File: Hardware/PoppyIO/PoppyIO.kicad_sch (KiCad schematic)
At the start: 244 parts, among them U11 74HC14, U12 74HC14

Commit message: hw: io: Different fuses
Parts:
- C29: value 100n -> (none); footprint Capacitor_SMD:C_0603_1608Metric_Pad1.08x0.95mm_HandSolder -> (none)
- F1, F10, F11, F12, F13, F14, F15, F16, F2, F3, F4, F5, F6, F7, F8, F9: Reichelt SKU PTC FSMD0302920R -> LITT 1210L010WR
- R74: footprint Resistor_SMD:R_0603_1608Metric -> (none)
- R75, R76, R77, R78, R79, R80, R81, R82, R83, R84, R85, R86, R87, R88, R89: value 10k -> (none); footprint Resistor_SMD:R_0603_1608Metric -> (none)
- U10, U11, U12: value 74HC14 -> (none); footprint Package_SO:SOIC-14_3.9x8.7mm_P1.27mm -> (none)
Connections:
- net O00_FIELD: now also F1.2; no longer F7.2
- net O01_FIELD: now also F2.2; no longer F6.2
- net O02_FIELD: now also F3.2; no longer F5.2
- net O04_FIELD: now also F5.2; no longer F3.2
- net O05_FIELD: now also F6.2; no longer F2.2
- net O06_FIELD: now also F7.2; no longer F1.2
- net O07_FIELD: now also F8.2; no longer F12.2
- net O08_FIELD: now also F9.2; no longer F11.2
- net O10_FIELD: now also F11.2; no longer F9.2
- net O11_FIELD: now also F12.2; no longer F8.2
- net O12_FIELD: now also F13.2; no longer F16.2
- net O13_FIELD: now also F14.2; no longer F15.2
- net O14_FIELD: now also F15.2; no longer F14.2
- net O15_FIELD: now also F16.2; no longer F13.2
- net at F11.1: now also U7.13 (O4); no longer U7.11 (O6)
- net at F6.1: now also U6.15 (O2); no longer U6.11 (O6)
- net at F8.1: now also U7.10 (O7); no longer U7.14 (O3)
- net at F13.1: now also U8.13 (O4); no longer U8.16 (O1)
- net at U6.10 (O7): now also F1.1; no longer F7.1
- net at U6.12 (O5): now also F3.1; no longer F5.1
- net at U6.14 (O3): now also F5.1; no longer F3.1
- net at F2.1: now also U6.11 (O6); no longer U6.15 (O2)
- net at U6.16 (O1): now also F7.1; no longer F1.1
- net at F15.1: now also U8.15 (O2); no longer U8.14 (O3)
- net at F14.1: now also U8.14 (O3); no longer U8.15 (O2)
- net at F16.1: now also U8.16 (O1); no longer U8.13 (O4)
- net at F12.1: now also U7.14 (O3); no longer U7.10 (O7)
- net at F9.1: now also U7.11 (O6); no longer U7.13 (O4)
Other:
- moved on the sheet: F1, F11, F12, F13, F14, F15, F16, F2, F3, F5, F6, F7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

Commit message: hw: io: Unused ULN2003 inputs
Tie them to GND.
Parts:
- C1: value (none) -> 10u; footprint (none) -> Capacitor_SMD:C_1210_3225Metric
- C10, C11, C12, C13, C14, C15, C16, C17, C18, C19, C20, C21, C22, C23, C8, C9: value (none) -> 1n; footprint (none) -> Capacitor_SMD:C_0805_2012Metric
- C2, C3: value (none) -> ~; footprint (none) -> Capacitor_SMD:C_0603_1608Metric_Pad1.08x0.95mm_HandSolder
- C24, C25, C26, C27, C28, C29, C4, C5, C6, C7: value (none) -> 100n; footprint (none) -> Capacitor_SMD:C_0603_1608Metric_Pad1.08x0.95mm_HandSolder
- D1: value (none) -> SKL14; footprint (none) -> Diode_SMD:D_SOD-123
- D10, D11, D12, D13, D14, D15, D16, D17, D18, D19, D20, D21, D22, D23, D24, D25, D26, D27, D28, D29, D3, D30, D31, D32, D33, D34, D4, D5, D6, D7, D8, D9: value (none) -> Green; footprint (none) -> LED_SMD:LED_0805_2012Metric_Pad1.15x1.40mm_HandSolder
- D2: value (none) -> SS14; footprint (none) -> Diode_SMD:D_SMA
- F1, F10, F11, F12, F13, F14, F15, F16, F2, F3, F4, F5, F6, F7, F8, F9: value (none) -> 30V 300mA; footprint (none) -> Fuse:Fuse_1210_3225Metric_Pad1.42x2.65mm_HandSolder
- H1, H2: value (none) -> MountingHole_Pad; footprint (none) -> MountingHole:MountingHole_3.2mm_M3_Pad_Via
- J1, J2, J3, J4, J5, J6, J7, J8: value (none) -> WAGO 233-504; footprint (none) -> PoppyLogicController:WAGO_233-204
- J10, J9: value (none) -> Phoenix MPT 0,5/ 4-2,54; footprint (none) -> TerminalBlock_Phoenix:TerminalBlock_Phoenix_MPT-0,5-4-2.54_1x04_P2.54mm_Horizontal
- J11: value (none) -> TC2030-IDC; footprint (none) -> Connector:Tag-Connect_TC2030-IDC-FP_2x03_P1.27mm_Vertical
- J12: value (none) -> Conn_02x06_Odd_Even; footprint (none) -> Connector_IDC:IDC-Header_2x06_P2.54mm_Vertical
- JP1: value (none) -> ~; footprint (none) -> Connector_PinHeader_2.54mm:PinHeader_1x02_P2.54mm_Vertical
- JP10, JP11, JP2, JP3, JP4, JP5, JP6, JP7, JP8, JP9: value (none) -> SolderJumper_2_Bridged; footprint (none) -> Jumper:SolderJumper-2_P1.3mm_Bridged_RoundedPad1.0x1.5mm
- R1, R2, R73: value (none) -> 0R; footprint (none) -> Resistor_SMD:R_0603_1608Metric
- R10, R11, R12, R21, R22, R23, R24, R33, R34, R35, R36, R45, R46, R47, R48, R9: value (none) -> 680 250mW; footprint (none) -> Resistor_SMD:R_1206_3216Metric
- R13, R14, R15, R16, R25, R26, R27, R28, R37, R38, R39, R40, R49, R50, R51, R52, R53, R54, R55, R56, R57, R58, R59, R60, R61, R62, R63, R64, R65, R66, R67, R68: value (none) -> 1k; footprint (none) -> Resistor_SMD:R_0603_1608Metric
- R17, R18, R19, R20, R29, R30, R31, R32, R41, R42, R43, R44, R5, R6, R7, R8: value (none) -> 3.3k 250mW; footprint (none) -> Resistor_SMD:R_1206_3216Metric
- R3, R4, R69, R70, R74, R75, R76, R77, R78, R79, R80, R81, R82, R83, R84, R85, R86, R87, R88, R89: value (none) -> 10k; footprint (none) -> Resistor_SMD:R_0603_1608Metric
- R71, R72: value (none) -> 4.7k; footprint (none) -> Resistor_SMD:R_0603_1608Metric_Pad0.98x0.95mm_HandSolder
- SW1: value (none) -> PTS645SH43SMTR92LFS; footprint (none) -> Button_Switch_SMD:SW_SPST_PTS645
- TP1, TP10, TP11, TP12, TP13, TP14, TP15, TP16, TP17, TP18, TP19, TP2, TP20, TP21, TP22, TP23, TP24, TP25, TP26, TP27, TP28, TP29, TP3, TP30, TP31, TP32, TP33, TP34, TP35, TP36, TP4, TP5, TP6, TP7, TP8, TP9: value (none) -> TestPoint_Small; footprint (none) -> TestPoint:TestPoint_Pad_D1.5mm
- TP37, TP38: value (none) -> TestPoint; footprint (none) -> TestPoint:TestPoint_Pad_D1.5mm
- U1: value (none) -> Pico; footprint (none) -> RPi_Pico:RPi_Pico_SMD_TH
- U10, U11, U12, U9: value (none) -> 74HC14; footprint (none) -> Package_SO:SOIC-14_3.9x8.7mm_P1.27mm
- U2, U3, U4, U5: value (none) -> PCA9538PW; footprint (none) -> Package_SO:TSSOP-16_4.4x5mm_P0.65mm
- U6, U7, U8: value (none) -> ULN2003AD; footprint (none) -> Package_SO:SOIC-16_3.9x9.9mm_P1.27mm
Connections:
- net GND: now also U7.1 (I1), U7.2 (I2), U8.5 (I5), U8.6 (I6), U8.7 (I7)
- no-connect marks 44 -> 39

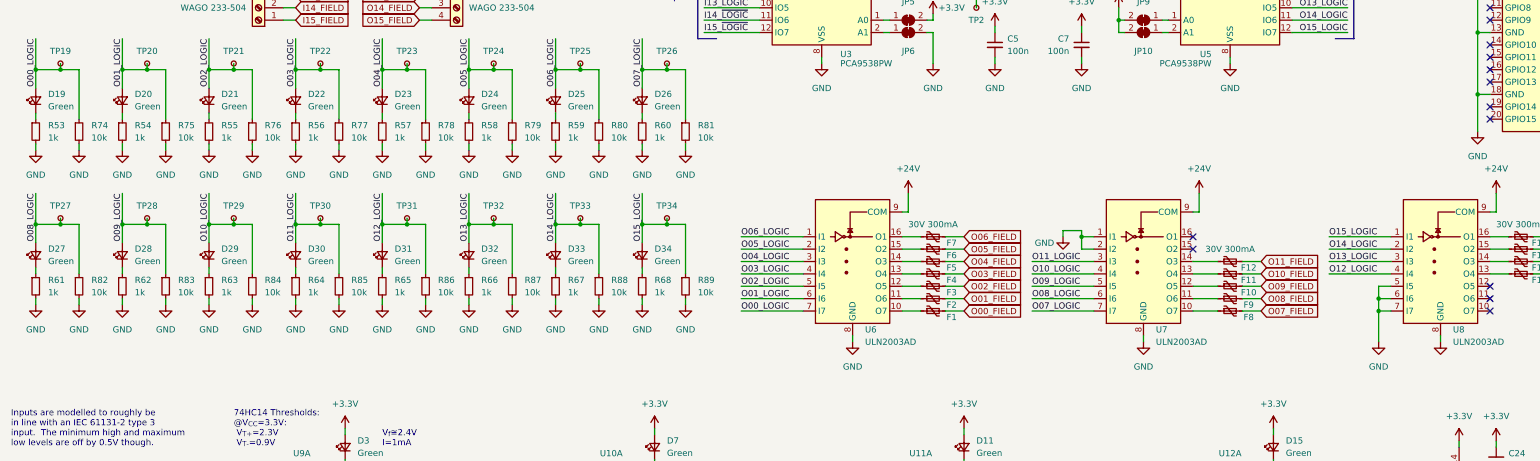
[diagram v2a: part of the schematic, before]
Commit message: hw: io: sch: Reorder series resistors for output LEDs
This helps with routing.
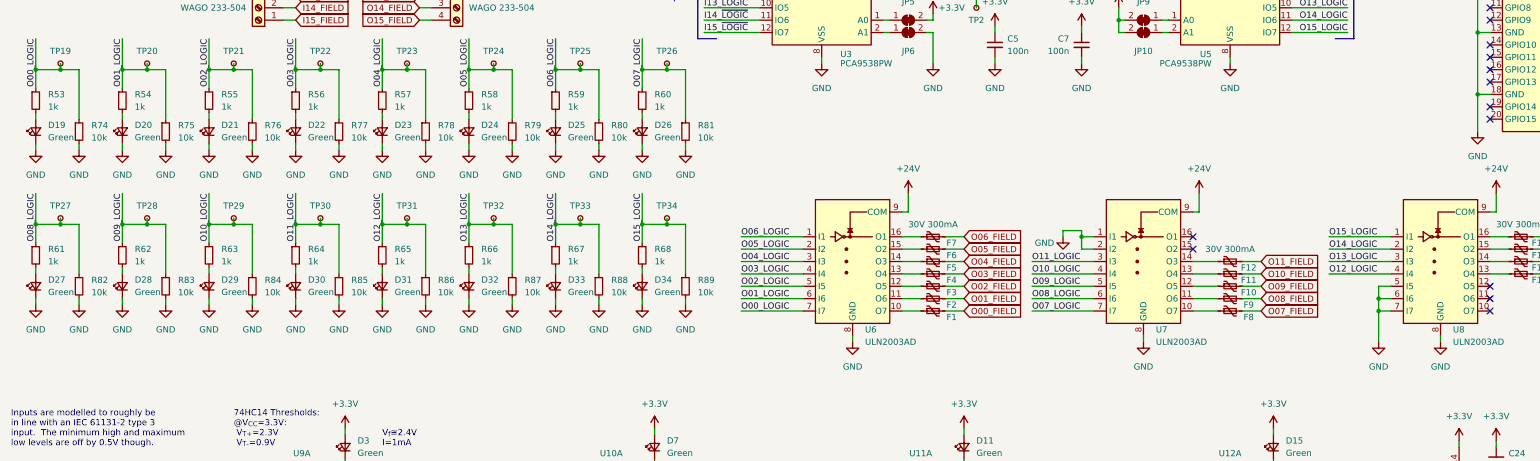
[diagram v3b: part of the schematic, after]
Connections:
- net GND: now also D19.1 (K), D20.1 (K), D21.1 (K), D22.1 (K), D23.1 (K), D24.1 (K), D25.1 (K), D26.1 (K), D27.1 (K), D28.1 (K), D29.1 (K), D30.1 (K), D31.1 (K), D32.1 (K), D33.1 (K), D34.1 (K); no longer R53.2, R54.2, R55.2, R56.2, R57.2, R58.2, R59.2, R60.2, R61.2, R62.2, R63.2, R64.2, R65.2, R66.2, R67.2, R68.2
- net O00_LOGIC: now also R53.1; no longer D19.2 (A)
- net O01_LOGIC: now also R54.1; no longer D20.2 (A)
- net O02_LOGIC: now also R55.1; no longer D21.2 (A)
- net O03_LOGIC: now also R56.1; no longer D22.2 (A)
- net O04_LOGIC: now also R57.1; no longer D23.2 (A)
- net O05_LOGIC: now also R58.1; no longer D24.2 (A)
- net O06_LOGIC: now also R59.1; no longer D25.2 (A)
- net O07_LOGIC: now also R60.1; no longer D26.2 (A)
- net O08_LOGIC: now also R61.1; no longer D27.2 (A)
- net O09_LOGIC: now also R62.1; no longer D28.2 (A)
- net O10_LOGIC: now also R63.1; no longer D29.2 (A)
- net O11_LOGIC: now also R64.1; no longer D30.2 (A)
- net O12_LOGIC: now also R65.1; no longer D31.2 (A)
- net O13_LOGIC: now also R66.1; no longer D32.2 (A)
- net O14_LOGIC: now also R67.1; no longer D33.2 (A)
- net O15_LOGIC: now also R68.1; no longer D34.2 (A)
- new net: D31.2 (A), R65.2
- new net: D23.2 (A), R57.2
- new net: D26.2 (A), R60.2
- new net: D19.2 (A), R53.2
- new net: D22.2 (A), R56.2
- new net: D24.2 (A), R58.2
- new net: D21.2 (A), R55.2
- new net: D33.2 (A), R67.2
- new net: D29.2 (A), R63.2
- new net: D32.2 (A), R66.2
- new net: D25.2 (A), R59.2
- new net: D28.2 (A), R62.2
- new net: D20.2 (A), R54.2
- new net: D34.2 (A), R68.2
- new net: D27.2 (A), R61.2
- new net: D30.2 (A), R64.2
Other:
- moved on the sheet: D19, D20, D21, D22, D23, D24, D25, D26, D27, D28, D29, D30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

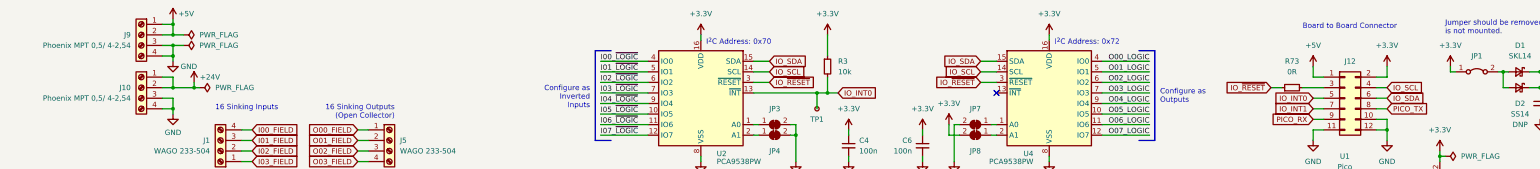
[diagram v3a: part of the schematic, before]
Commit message: hw: io: More PCB layout
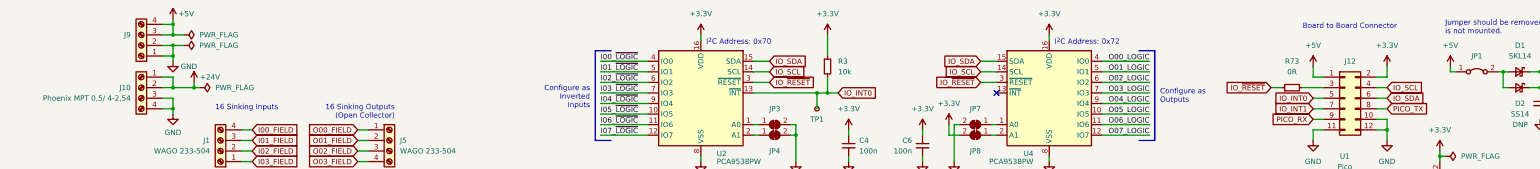
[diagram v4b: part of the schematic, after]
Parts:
- J9: value Phoenix MPT 0,5/ 4-2,54 -> (none); footprint TerminalBlock_Phoenix:TerminalBlock_Phoenix_MPT-0,5-4-2.54_1x04_P2.54mm_Horizontal -> (none)
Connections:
- net +3V3: no longer JP1.1 (A)
- net +5V: now also J9.3 (Pin_3), J9.4 (Pin_4), JP1.1 (A); no longer J9.1 (Pin_1), J9.2 (Pin_2)
- net GND: now also J9.1 (Pin_1), J9.2 (Pin_2); no longer J9.3 (Pin_3), J9.4 (Pin_4)
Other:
- moved on the sheet: J9
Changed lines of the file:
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@@
     (pin "1")
   )
-  (symbol (lib_id "Connector:Screw_Terminal_01x04") (at 46.99 20.32 0) (mirror y) (unit 1)
-    (in_bom yes) (on_board yes) (fields_autoplaced)
-    (property "Reference" "J9" (id 0) (at 44.45 20.3199 0)
+  (symbol (lib_id "Connector:Screw_Terminal_01x04") (at 46.99 22.86 180) (unit 1)
+    (in_bom yes) (on_board yes)
+    (property "Reference" "J9" (id 0) (at 44.45 20.32 0)
       (effects (font (size 1.27 1.27)) (justify left))
     )
-    (property "Value" "Phoenix MPT 0,5/ 4-2,54" (id 1) (at 44.45 22.8599 0)
+    (property "Value" "" (id 1) (at 44.45 22.86 0)
       (effects (font (size 1.27 1.27)) (justify left))
     )
-    (property "Footprint" "TerminalBlock_Phoenix:TerminalBlock_Phoenix_MPT-0,5-4-2.54_1x04_P2.54mm_Horizontal" (id 2) (at 46.99 20.32 0)
+    (property "Footprint" "" (id 2) (at 46.99 22.86 0)
       (effects (font (size 1.27 1.27)) hide)
     )
-    (property "Datasheet" "~" (id 3) (at 46.99 20.32 0)
+    (property "Datasheet" "~" (id 3) (at 46.99 22.86 0)
       (effects (font (size 1.27 1.27)) hide)
     )
@@
     (pin "1")
   )
-  (symbol (lib_id "power:+3.3V") (at 361.95 27.94 0) (unit 1)
-    (in_bom yes) (on_board yes) (fields_autoplaced)
-    (property "Reference" "#PWR0131" (id 0) (at 361.95 31.75 0)
-      (effects (font (size 1.27 1.27)) hide)
-    )
-    (property "Value" "+3.3V" (id 1) (at 361.95 22.86 0))
-    (property "Footprint" "" (id 2) (at 361.95 27.94 0)
-      (effects (font (size 1.27 1.27)) hide)
-    )
-    (property "Datasheet" "" (id 3) (at 361.95 27.94 0)
-      (effects (font (size 1.27 1.27)) hide)
-    )
-    (pin "1")
-  )
   (symbol (lib_id "Device:C_Small") (at 320.04 215.9 0) (unit 1)
     (in_bom yes) (on_board yes) (fields_autoplaced)
@@
     (pin "2")
   )
+  (symbol (lib_id "power:+5V") (at 361.95 27.94 0) (unit 1)
+    (in_bom yes) (on_board yes) (fields_autoplaced)
+    (property "Reference" "#PWR?" (id 0) (at 361.95 31.75 0)
+      (effects (font (size 1.27 1.27)) hide)
+    )
+    (property "Value" "+5V" (id 1) (at 361.95 22.86 0))
+    (property "Footprint" "" (id 2) (at 361.95 27.94 0)
+      (effects (font (size 1.27 1.27)) hide)
+    )
+    (property "Datasheet" "" (id 3) (at 361.95 27.94 0)
+      (effects (font (size 1.27 1.27)) hide)
+    )
+    (pin "1")
+  )
   (symbol (lib_id "Device:R_Small") (at 57.15 255.27 90) (unit 1)
     (in_bom yes) (on_board yes) (fields_autoplaced)
@@
       (reference "#PWR0130") (unit 1) (value "GND") (footprint "")
     )
-    (path "/d4c8f4f6-c1cb-4be5-a931-c374a21e16e2"
-      (reference "#PWR0131") (unit 1) (value "+3.3V") (footprint "")
-    )
     (path "/fb0963c8-0aa6-46ce-85a9-5d5af03b6001"
       (reference "#PWR0132") (unit 1) (value "+3.3V") (footprint "")
@@
       (reference "#PWR0143") (unit 1) (value "GND") (footprint "")
     )
+    (path "/f9200ee4-0053-410d-bc5c-53542c90d30e"
+      (reference "#PWR?") (unit 1) (value "+5V") (footprint "")
+    )
     (path "/b9ac49ae-7d34-4ed6-a926-b142ee48d81a"
